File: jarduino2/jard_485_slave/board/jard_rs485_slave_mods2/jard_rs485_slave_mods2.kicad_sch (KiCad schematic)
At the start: 0 parts

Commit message: Finitions avant production
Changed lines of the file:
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@@
     (comment 3 "1 sortie 12V/5A - 2 entrées TOR - 1 débimètre - 1 LED - Temp - RS485")
   )
-  (text_box "Version F0:\n\n- Déplacement piste LED trop proche du bord\n- Inversion TX/RX"
-    (at 33.02 165.1 0) (size 66.04 13.97)
+  (text_box "Version G0:\n- Remplacement module RS485 par MAX485E\n- Ajout d'un cavalier pour couper RX pendant la programation via USB\n\nVersion F0:\n- Déplacement piste LED trop proche du bord\n- Inversion TX/RX"
+    (at 26.67 158.75 0) (size 72.39 19.05)
     (stroke (width 0) (type default))
     (fill (type none))
@@
     (effects (font (face "Arial") (size 10 10)) (justify left bottom))
   )
-  (sheet (at 92.71 105.41) (size 54.61 39.37) (fields_autoplaced)
+  (sheet (at 91.44 93.98) (size 54.61 39.37) (fields_autoplaced)
     (stroke (width 0.1524) (type solid))
     (fill (color 255 194 126 1.0000))
-    (property "Sheetname" "UC" (at 92.71 104.6984 0)
+    (property "Sheetname" "UC" (at 91.44 93.2684 0)
       (effects (font (size 1.27 1.27)) (justify left bottom))
     )
-    (property "Sheetfile" "uc.kicad_sch" (at 92.71 145.3646 0)
+    (property "Sheetfile" "uc.kicad_sch" (at 91.44 133.9346 0)
       (effects (font (size 1.27 1.27)) (justify left top))
     )
@@
     )
   )
-  (sheet (at 171.45 105.41) (size 41.91 38.1) (fields_autoplaced)
+  (sheet (at 170.18 93.98) (size 41.91 38.1) (fields_autoplaced)
     (stroke (width 0.1524) (type solid))
     (fill (color 153 145 255 1.0000))
-    (property "Sheetname" "ES" (at 171.45 104.6984 0)
+    (property "Sheetname" "ES" (at 170.18 93.2684 0)
       (effects (font (size 1.27 1.27)) (justify left bottom))
     )
-    (property "Sheetfile" "ES.kicad_sch" (at 171.45 144.0946 0)
+    (property "Sheetfile" "ES.kicad_sch" (at 170.18 132.6646 0)
       (effects (font (size 1.27 1.27)) (justify left top))
     )

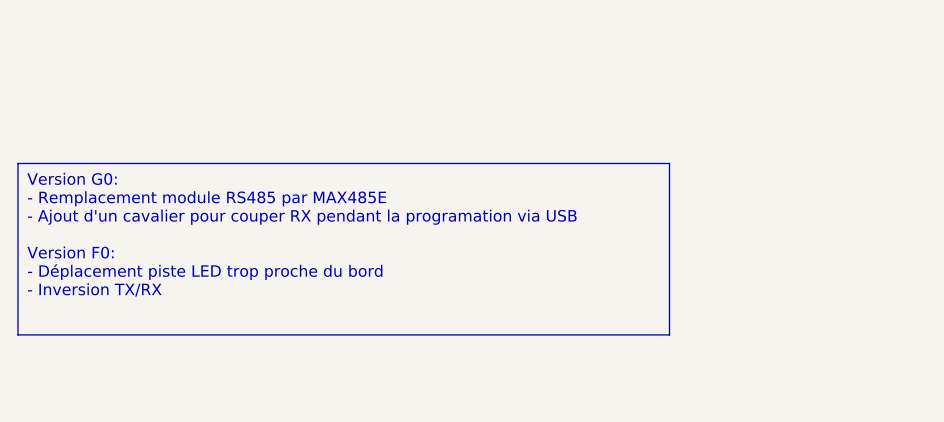
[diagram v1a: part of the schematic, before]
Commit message: Amélioration découplage RS485, MOS sur autre face
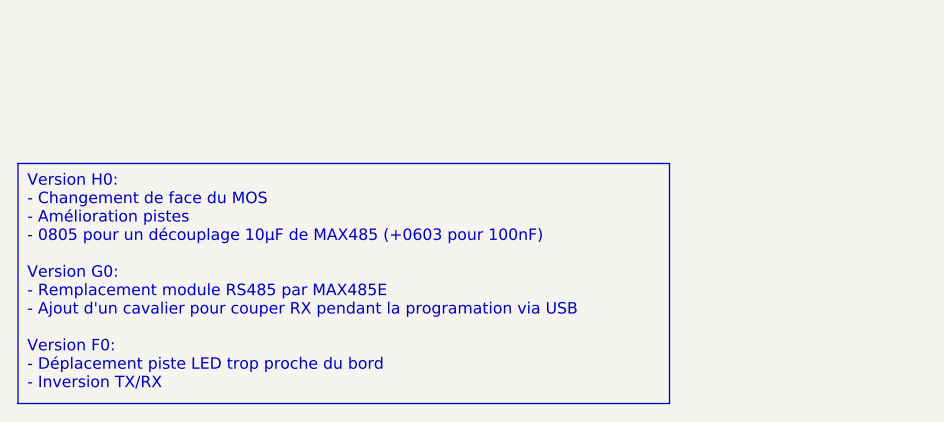
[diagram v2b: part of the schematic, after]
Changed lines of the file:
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@@
   (title_block
     (title "Carte de commande d'un OYA - Esclave RS485")
-    (date "2024-05-05")
-    (rev "G0")
+    (date "2024-06-11")
+    (rev "H0")
     (company "BPC")
-    (comment 1 "Technologie avec modules Arduino Nano / Petite carte")
+    (comment 1 "Technologie avec module Arduino Nano / Petite carte")
     (comment 2 "Monitoring de tension d'alimentation")
     (comment 3 "1 sortie 12V/5A - 2 entrées TOR - 1 débimètre - 1 LED - Temp - RS485")
   )
-  (text_box "Version G0:\n- Remplacement module RS485 par MAX485E\n- Ajout d'un cavalier pour couper RX pendant la programation via USB\n\nVersion F0:\n- Déplacement piste LED trop proche du bord\n- Inversion TX/RX"
-    (at 26.67 158.75 0) (size 72.39 19.05)
+  (text_box "Version H0:\n- Changement de face du MOS\n- Amélioration pistes\n- 0805 pour un découplage 10µF de MAX485 (+0603 pour 100nF)\n\nVersion G0:\n- Remplacement module RS485 par MAX485E\n- Ajout d'un cavalier pour couper RX pendant la programation via USB\n\nVersion F0:\n- Déplacement piste LED trop proche du bord\n- Inversion TX/RX"
+    (at 26.67 158.75 0) (size 72.39 26.67)
     (stroke (width 0) (type default))
     (fill (type none))
